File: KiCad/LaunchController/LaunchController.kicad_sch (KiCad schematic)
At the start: 32 parts, among them J1 CONN_ICSP, J2 CONN_USB, J3 USB_B_Micro, U1 FT232RL, U2 ATMEGA2560-16AUR, Y1 HUSG-16.000-20

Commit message: EDLCを削除
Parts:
- removed C4: 1F, Capacitor_THT:DX_5R5VxxxxU_D19.0mm_P5.00mm, symbol Device:C_Polarized_Small
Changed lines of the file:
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@@
     (company "Tokai Student Rocket Project")
   )
-  (junction (at 111.76 20.32) (diameter 0) (color 0 0 0 0)
-  )
   (junction (at 52.07 33.02) (diameter 0) (color 0 0 0 0)
   )
@@
   (junction (at 260.35 45.72) (diameter 0) (color 0 0 0 0)
   )
-  (junction (at 101.6 30.48) (diameter 0) (color 0 0 0 0)
+  (junction (at 101.6 20.32) (diameter 0) (color 0 0 0 0)
   )
   (junction (at 129.54 119.38) (diameter 0) (color 0 0 0 0)
@@
   )
   (junction (at 41.91 60.96) (diameter 0) (color 0 0 0 0)
-  )
-  (junction (at 101.6 20.32) (diameter 0) (color 0 0 0 0)
   )
   (junction (at 30.48 60.96) (diameter 0) (color 0 0 0 0)
@@
     (stroke (width 0) (type default))
   )
-  (wire (pts (xy 111.76 22.86) (xy 111.76 20.32))
-    (stroke (width 0) (type default))
-  )
   (wire (pts (xy 95.25 154.94) (xy 97.79 154.94))
     (stroke (width 0) (type default))
@@
     (stroke (width 0) (type default))
   )
-  (wire (pts (xy 111.76 17.78) (xy 111.76 20.32))
+  (wire (pts (xy 101.6 17.78) (xy 101.6 20.32))
     (stroke (width 0) (type default))
   )
@@
     (stroke (width 0) (type default))
   )
-  (wire (pts (xy 111.76 30.48) (xy 101.6 30.48))
-    (stroke (width 0) (type default))
-  )
   (wire (pts (xy 74.93 20.32) (xy 81.28 20.32))
     (stroke (width 0) (type default))
@@
     (stroke (width 0) (type default))
   )
-  (wire (pts (xy 111.76 27.94) (xy 111.76 30.48))
-    (stroke (width 0) (type default))
-  )
   (wire (pts (xy 52.07 165.1) (xy 54.61 165.1))
     (stroke (width 0) (type default))
@@
   )
   (wire (pts (xy 120.65 139.7) (xy 123.19 139.7))
-    (stroke (width 0) (type default))
-  )
-  (wire (pts (xy 101.6 20.32) (xy 111.76 20.32))
     (stroke (width 0) (type default))
   )
@@
         (path "/628d040b-43bf-4733-804f-091644a90124"
           (reference "#PWR02") (unit 1)
-        )
-      )
-    )
-  )
-  (symbol (lib_id "Device:C_Polarized_Small") (at 111.76 25.4 0) (unit 1)
-    (in_bom yes) (on_board yes) (dnp no)
-    (property "Reference" "C4" (at 114.3 24.2189 0)
-      (effects (font (size 1.27 1.27)) (justify left))
-    )
-    (property "Value" "1F" (at 114.3 26.7589 0)
-      (effects (font (size 1.27 1.27)) (justify left))
-    )
-    (property "Footprint" "Capacitor_THT:DX_5R5VxxxxU_D19.0mm_P5.00mm" (at 111.76 25.4 0)
-      (effects (font (size 1.27 1.27)) hide)
-    )
-    (property "Datasheet" "https://akizukidenshi.com/catalog/g/gP-04249/" (at 111.76 25.4 0)
-      (effects (font (size 1.27 1.27)) hide)
-    )
-    (property "LCSC" "" (at 111.76 25.4 0)
-      (effects (font (size 1.27 1.27)) hide)
-    )
-    (pin "1")
-    (pin "2")
-    (instances
-      (project "LaunchController"
-        (path "/628d040b-43bf-4733-804f-091644a90124"
-          (reference "C4") (unit 1)
         )
       )
@@
     )
   )
-  (symbol (lib_id "power:+5V") (at 111.76 17.78 0) (unit 1)
+  (symbol (lib_id "power:+5V") (at 101.6 17.78 0) (unit 1)
     (in_bom yes) (on_board yes) (dnp no)
-    (property "Reference" "#PWR01" (at 111.76 21.59 0)
-      (effects (font (size 1.27 1.27)) hide)
-    )
-    (property "Value" "+5V" (at 111.76 13.97 0)
-      (effects (font (size 1.27 1.27)))
-    )
-    (property "Footprint" "" (at 111.76 17.78 0)
-      (effects (font (size 1.27 1.27)) hide)
-    )
-    (property "Datasheet" "" (at 111.76 17.78 0)
-      (effects (font (size 1.27 1.27)) hide)
-    )
+    (property "Reference" "#PWR01" (at 101.6 21.59 0)
+      (effects (font (size 1.27 1.27)) hide)
+    )
+    (property "Value" "+5V" (at 101.6 13.97 0)
+      (effects (font (size 1.27 1.27)))
+    )
+    (property "Footprint" "" (at 101.6 17.78 0)
+      (effects (font (size 1.27 1.27)) hide)
+    )
+    (property "Datasheet" "" (at 101.6 17.78 0)
+      (effects (font (size 1.27 1.27)) hide)
+    )

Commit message: TVSダイオードの極性が逆だったので修正
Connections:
- net GND: now also D2.2 (A2), D3.2 (A2); no longer D2.1 (A1), D3.1 (A1)
- net USB_D+: now also D2.1 (A1); no longer D2.2 (A2)
- net USB_D-: now also D3.1 (A1); no longer D3.2 (A2)
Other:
- moved on the sheet: D2, D3
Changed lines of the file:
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@@
     )
   )
-  (symbol (lib_id "Diode:SM6T200A") (at 172.72 52.07 90) (unit 1)
-    (in_bom yes) (on_board yes) (dnp no)
-    (property "Reference" "D3" (at 175.26 52.07 90)
-      (effects (font (size 1.27 1.27)) (justify right))
-    )
-    (property "Value" "SMAJ45A" (at 175.26 54.61 90)
-      (effects (font (size 1.27 1.27)) (justify right))
-    )
-    (property "Footprint" "Diode_SMD:D_SMA_Handsoldering" (at 177.8 52.07 0)
-      (effects (font (size 1.27 1.27)) hide)
-    )
-    (property "Datasheet" "https://akizukidenshi.com/catalog/g/gI-07409/" (at 172.72 53.34 0)
+  (symbol (lib_id "Diode:SM6T200A") (at 172.72 52.07 270) (unit 1)
+    (in_bom yes) (on_board yes) (dnp no)
+    (property "Reference" "D3" (at 175.26 53.34 90)
+      (effects (font (size 1.27 1.27)) (justify left))
+    )
+    (property "Value" "SMAJ45A" (at 175.26 50.8 90)
+      (effects (font (size 1.27 1.27)) (justify left))
+    )
+    (property "Footprint" "Diode_SMD:D_SMA_Handsoldering" (at 167.64 52.07 0)
+      (effects (font (size 1.27 1.27)) hide)
+    )
+    (property "Datasheet" "https://akizukidenshi.com/catalog/g/gI-07409/" (at 172.72 50.8 0)
       (effects (font (size 1.27 1.27)) hide)
     )
@@
     )
   )
-  (symbol (lib_id "Diode:SM6T200A") (at 167.64 52.07 90) (unit 1)
-    (in_bom yes) (on_board yes) (dnp no)
-    (property "Reference" "D2" (at 165.1 52.07 90)
-      (effects (font (size 1.27 1.27)) (justify left))
-    )
-    (property "Value" "SMAJ45A" (at 165.1 54.61 90)
-      (effects (font (size 1.27 1.27)) (justify left))
-    )
-    (property "Footprint" "Diode_SMD:D_SMA_Handsoldering" (at 172.72 52.07 0)
-      (effects (font (size 1.27 1.27)) hide)
-    )
-    (property "Datasheet" "https://akizukidenshi.com/catalog/g/gI-07409/" (at 167.64 53.34 0)
-      (effects (font (size 1.27 1.27)) hide)
-    )
+  (symbol (lib_id "Diode:SM6T200A") (at 167.64 52.07 270) (unit 1)
+    (in_bom yes) (on_board yes) (dnp no)
+    (property "Reference" "D2" (at 165.1 53.34 90)
+      (effects (font (size 1.27 1.27)) (justify right))
+    )
+    (property "Value" "SMAJ45A" (at 165.1 50.8 90)
+      (effects (font (size 1.27 1.27)) (justify right))
+    )
+    (property "Footprint" "Diode_SMD:D_SMA_Handsoldering" (at 162.56 52.07 0)
+      (effects (font (size 1.27 1.27)) hide)
+    )
+    (property "Datasheet" "https://akizukidenshi.com/catalog/g/gI-07409/" (at 167.64 50.8 0)
+      (effects (font (size 1.27 1.27)) hide)
+    )

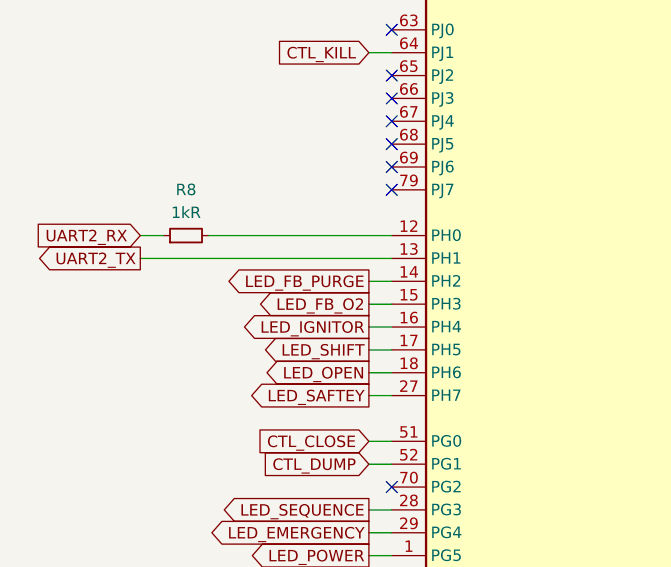
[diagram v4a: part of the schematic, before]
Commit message: DFPlayerのTXにも抵抗を追加
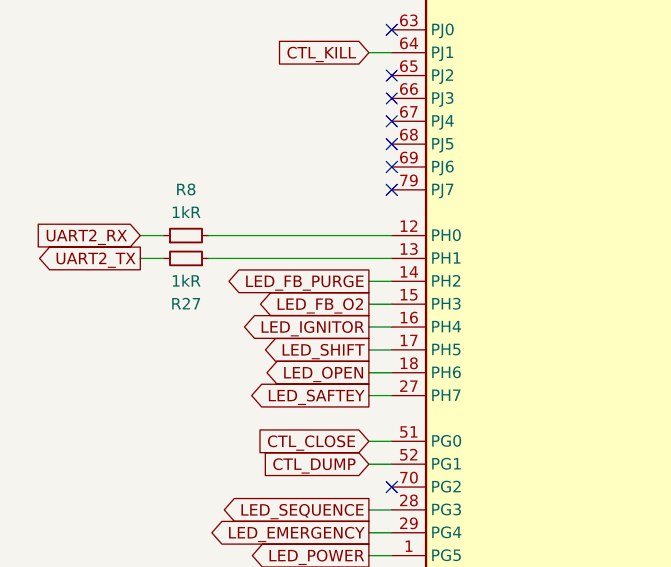
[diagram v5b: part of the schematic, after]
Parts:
- added R27: 1kR, Resistor_SMD:R_0603_1608Metric_Pad0.98x0.95mm_HandSolder, symbol Device:R_Small
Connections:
- net UART2_TX: now also R27.2; no longer U2.13 (PH1)
- new net: R27.1, U2.13 (PH1)
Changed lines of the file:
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@@
     (stroke (width 0) (type default))
   )
-  (wire (pts (xy 26.67 142.24) (xy 54.61 142.24))
+  (wire (pts (xy 26.67 142.24) (xy 29.21 142.24))
     (stroke (width 0) (type default))
   )
@@
   )
   (wire (pts (xy 172.72 58.42) (xy 172.72 55.88))
+    (stroke (width 0) (type default))
+  )
+  (wire (pts (xy 34.29 142.24) (xy 54.61 142.24))
     (stroke (width 0) (type default))
   )
@@
         )
       )
+    )
+  )
+  (symbol (lib_id "Device:R_Small") (at 31.75 142.24 270) (mirror x) (unit 1)
+    (in_bom yes) (on_board yes) (dnp no)
+    (property "Reference" "R27" (at 31.75 147.32 90)
+      (effects (font (size 1.27 1.27)))
+    )
+    (property "Value" "1kR" (at 31.75 144.78 90)
+      (effects (font (size 1.27 1.27)))
+    )
+    (property "Footprint" "Resistor_SMD:R_0603_1608Metric_Pad0.98x0.95mm_HandSolder" (at 31.75 142.24 0)
+      (effects (font (size 1.27 1.27)) hide)
+    )
+    (property "Datasheet" "https://www.chip1stop.com/view/dispDetail/DispDetail?partId=ROHM-0021097" (at 31.75 142.24 0)
+      (effects (font (size 1.27 1.27)) hide)
+    )
+    (property "LCSC" "" (at 31.75 142.24 0)
+      (effects (font (size 1.27 1.27)) hide)
+    )
+    (pin "1")
+    (pin "2")
+    (instances
+      (project "LaunchController"
+        (path "/628d040b-43bf-4733-804f-091644a90124"
+          (reference "R27") (unit 1)
+        )
+      )

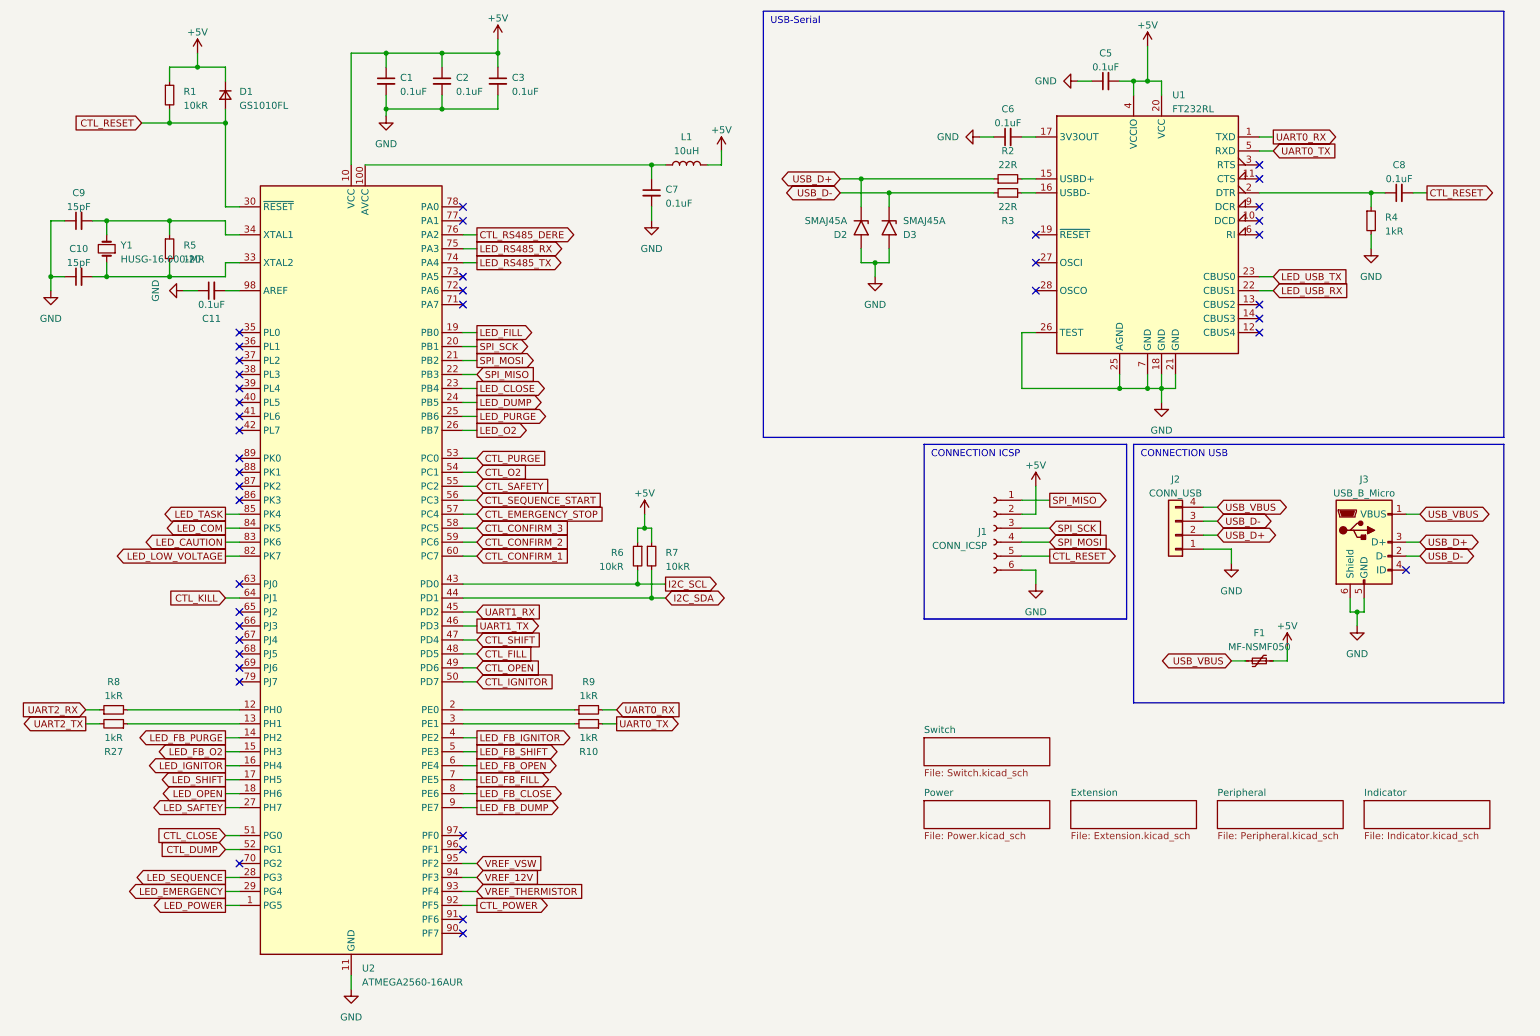
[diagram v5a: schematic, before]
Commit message: 7セグ制御端子を追加
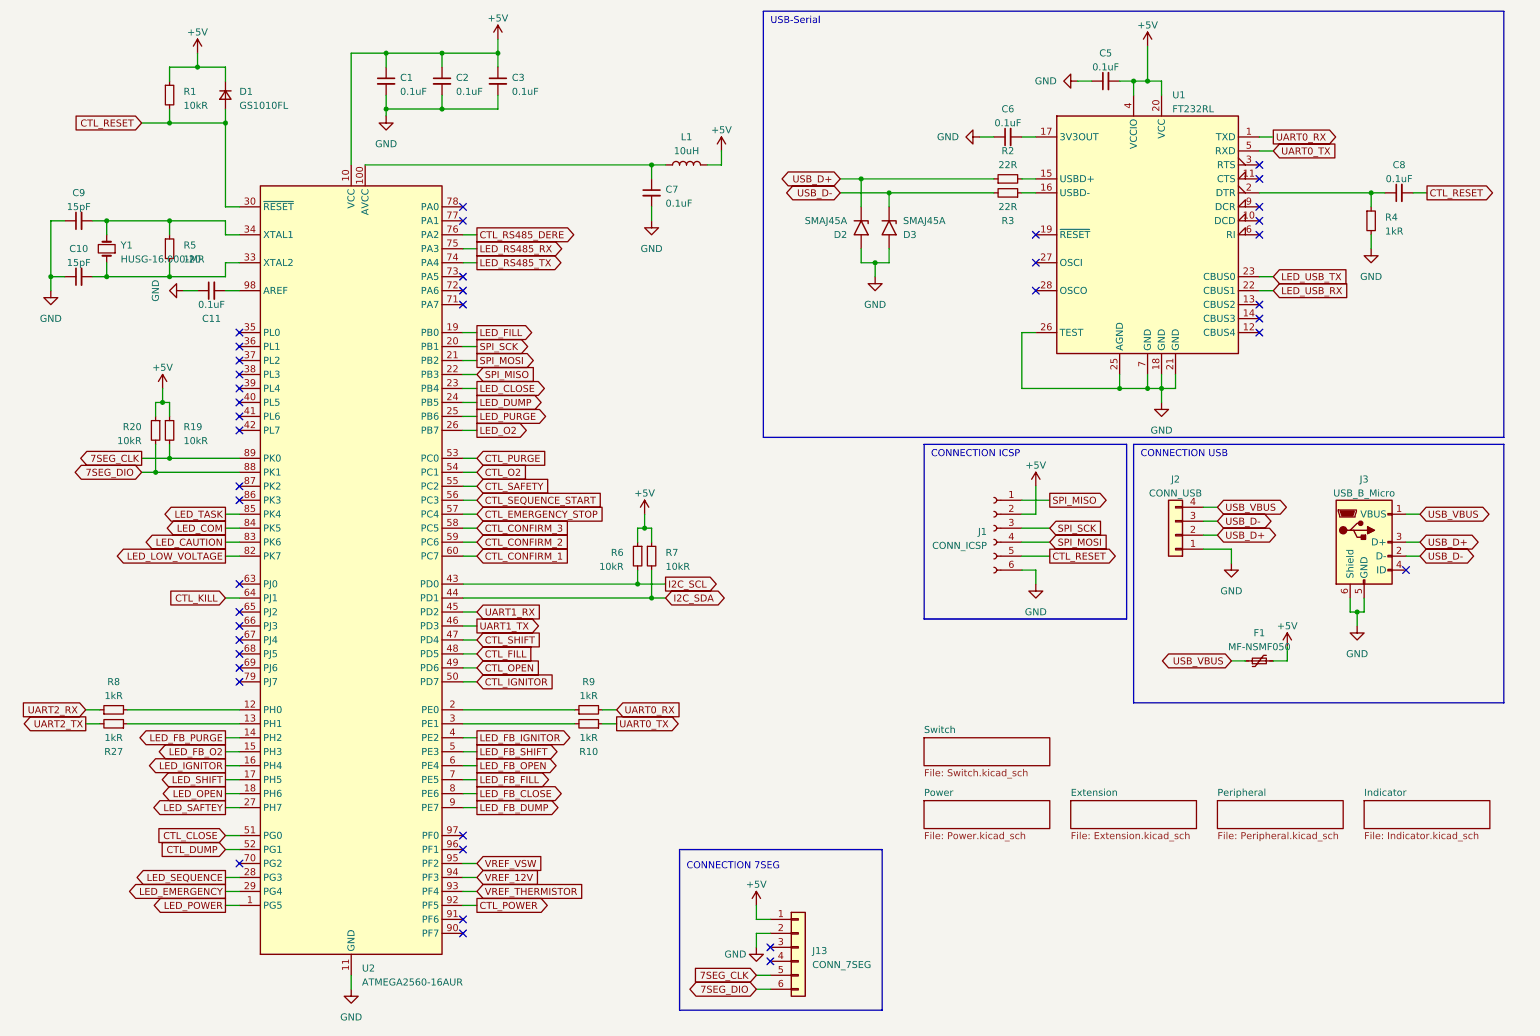
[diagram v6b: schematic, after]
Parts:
- added J13: CONN_7SEG, TSRP_Connector_Hirose:DF51A-6DP-2DSA, symbol Connector_Generic:Conn_01x06
- added R19, R20: 10kR, Resistor_SMD:R_0603_1608Metric_Pad0.98x0.95mm_HandSolder, symbol Device:R_Small
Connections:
- net +5V: now also J13.1 (Pin_1), R19.1, R20.1
- net GND: now also J13.2 (Pin_2)
- net 7SEG_DIO: now reaches U2.88 (PK1)
- net 7SEG_DIO: now also J13.6 (Pin_6), R20.2
- net 7SEG_CLK: now reaches U2.89 (PK0)
- net 7SEG_CLK: now also J13.5 (Pin_5), R19.2
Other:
- note added: "CONNECTION 7SEG"

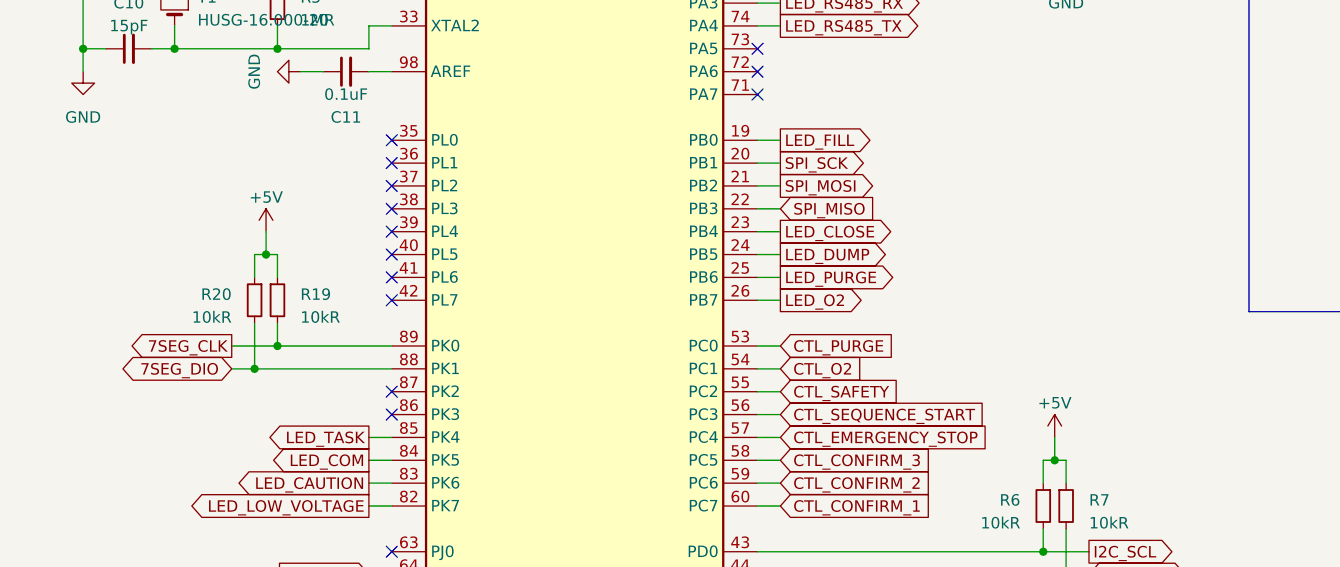
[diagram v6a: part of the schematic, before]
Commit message: LED_BUILDINを避難
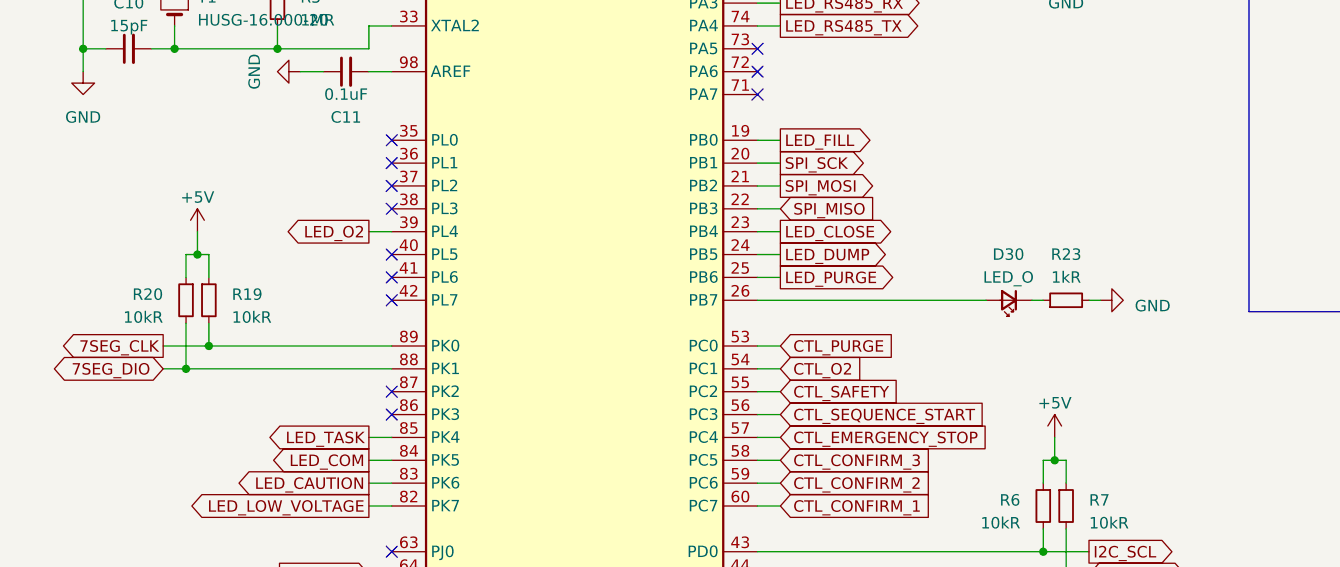
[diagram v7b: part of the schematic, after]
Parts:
- added D30: LED_O, LED_SMD:LED_0603_1608Metric_Pad1.05x0.95mm_HandSolder, symbol Device:LED_Small
- added R23: 1kR, Resistor_SMD:R_0603_1608Metric_Pad0.98x0.95mm_HandSolder, symbol Device:R_Small
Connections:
- net GND: now also R23.2
- net LED_O2: now also U2.39 (PL4); no longer U2.26 (PB7)
- new net: D30.2 (A), U2.26 (PB7)
- new net: D30.1 (K), R23.1
- no-connect marks 41 -> 40
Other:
- moved on the sheet: R19, R20
